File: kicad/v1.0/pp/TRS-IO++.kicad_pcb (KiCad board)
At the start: 2 copper layers, 145.7 x 107.8 mm, 104 parts, among them J1 TRS-80 M3 Pin Header, J10 Cassette Input, J11 Mini-DIN-6, J12 USB_B_Micro, J13 UART, J2 TRS-80 M1 Pin Header, J3 TRS-80 M3 Edge Connector, J4 TRS-80 M1 Edge Connector, J5 Conn_02x06_Odd_Even, J6 Cassette Output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

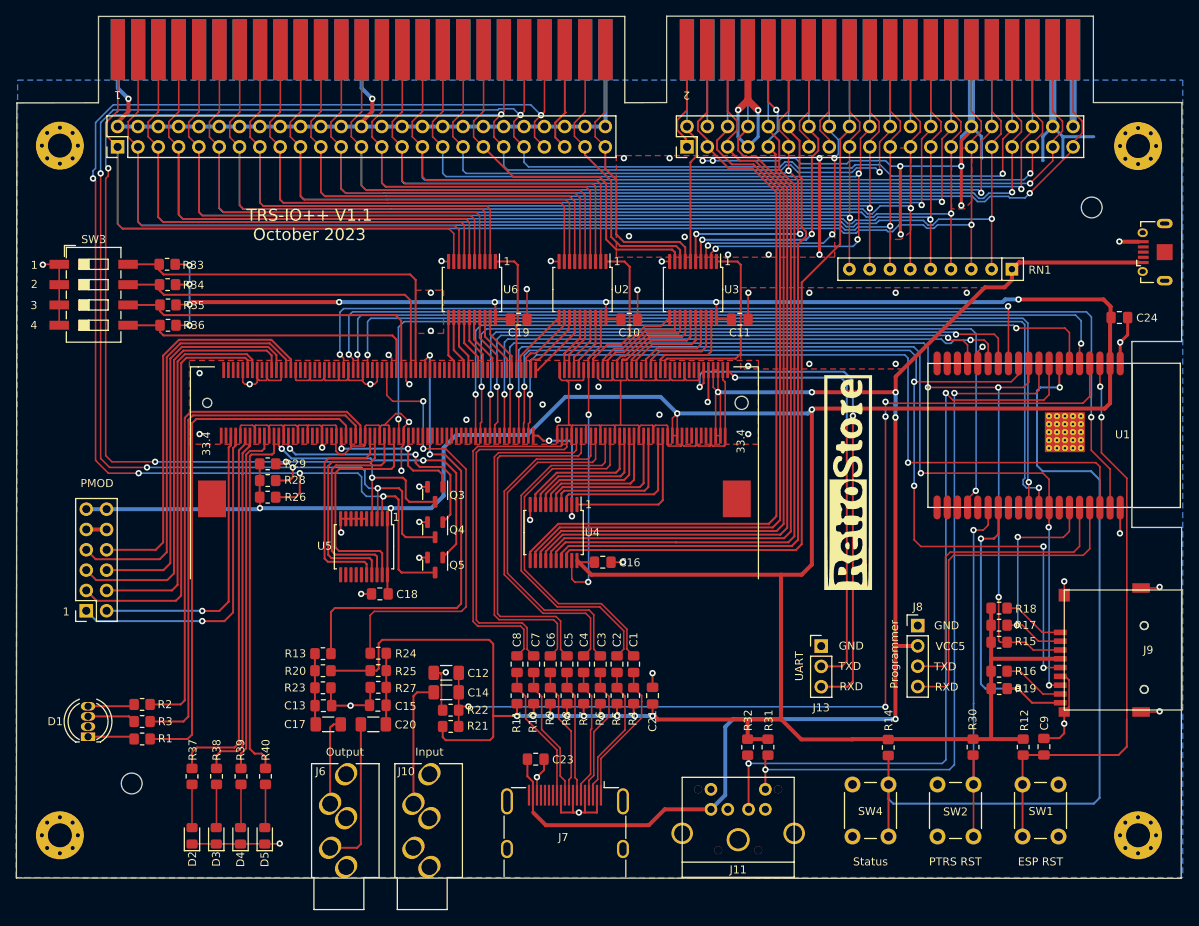
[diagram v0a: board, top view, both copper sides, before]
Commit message: Custom TRS-IO++ PCB (incomplete, no video)
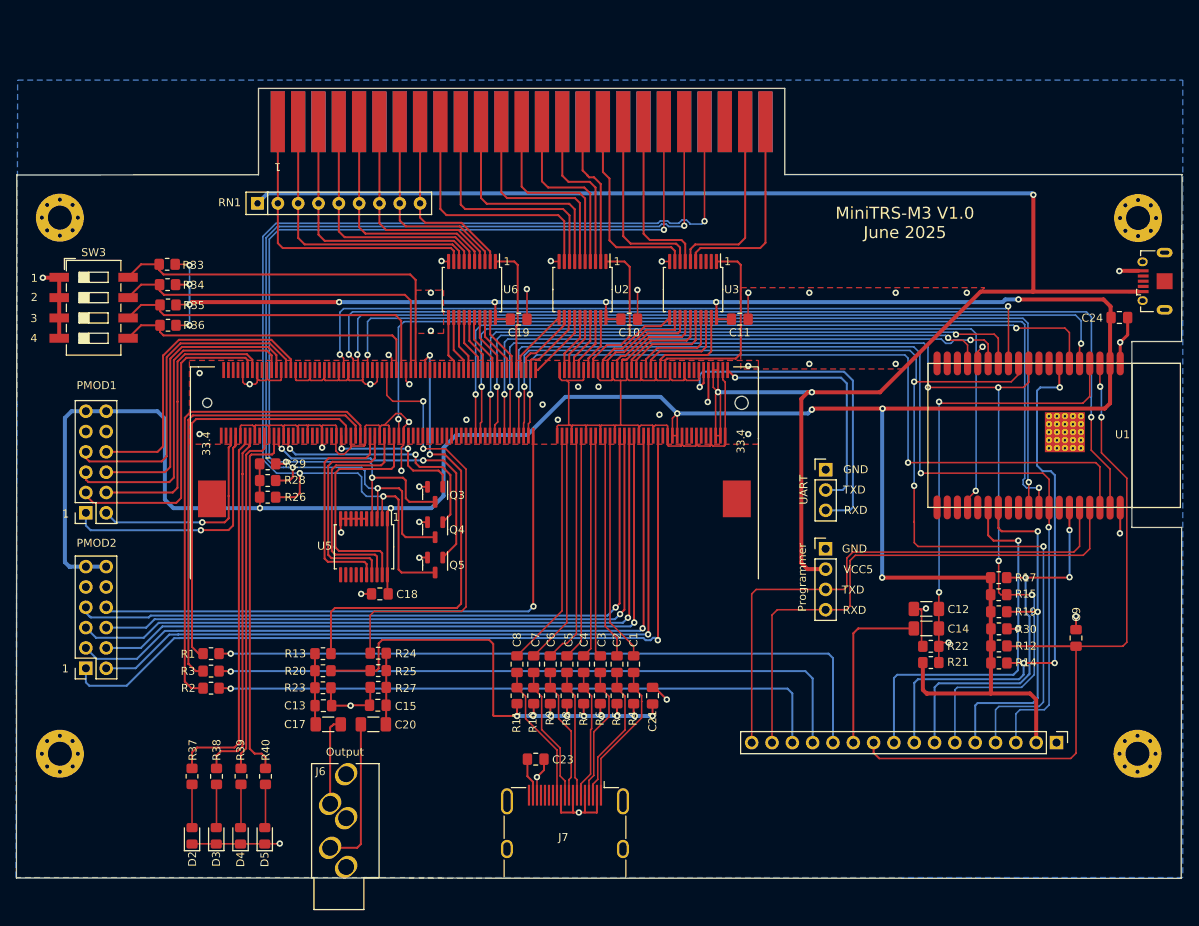
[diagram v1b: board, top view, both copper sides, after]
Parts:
- removed C16: 0.1uF, Capacitor_SMD:C_0805_2012Metric_Pad1.18x1.45mm_HandSolder
- removed D1: LED_RKBG, LED_THT:LED_D5.0mm-4_RGB
- removed G***, G1: LOGO, LOGO
- removed H5, H6: MountingHole, PocketTRS_Connectors:Alignment_Hole_2.6mm
- removed J10: Cassette Input, PocketTRS_Connectors:Jack_3.5mm_CUI_SJ1-3535NG_Horizontal_CircularHoles
- removed J11: Mini-DIN-6, PocketTRS_Connectors:minidin_6_ps2_pcb_mount
- removed J4: TRS-80 M1 Edge Connector, trs-io-m1:TRSEDGE
- removed J9: SD_Card, PocketTRS_Connectors:TFP09-2-12B
- removed R16, R18: 10K, Resistor_SMD:R_0805_2012Metric_Pad1.20x1.40mm_HandSolder
- removed R31, R32: 2K, Resistor_SMD:R_0805_2012Metric_Pad1.20x1.40mm_HandSolder
- removed SW1: ESP_RESET, Button_Switch_THT:SW_PUSH_6mm
- removed SW2: PTRS_RESET, Button_Switch_THT:SW_PUSH_6mm
- removed SW4: TRS_IO_STATUS, Button_Switch_THT:SW_PUSH_6mm
- removed U4: 74LVC245, trs-io-m3:SSOP-20_5.3x7.2mm_P0.65mm_slim
- J1: value TRS-80 M3 Pin Header -> Conn_02x06_Odd_Even; footprint Connector_PinHeader_2.54mm:PinHeader_2x25_P2.54mm_Vertical -> Connector_PinSocket_2.54mm:PinSocket_2x06_P2.54mm_Vertical
- J2: value TRS-80 M1 Pin Header -> Conn_01x16; footprint Connector_PinHeader_2.54mm:PinHeader_2x20_P2.54mm_Vertical -> Connector_PinHeader_2.54mm:PinHeader_1x16_P2.54mm_Vertical
- moved RN1 94.7 mm to (90.7, 62.5), turned to 0 degrees
- moved J2 87.6 mm to (190.6, 129.9), turned to -90 degrees
- moved J1 65.3 mm to (69.3, 120.6), turned to 180 degrees
- moved C12 60.5 mm to (174.3, 113.2)
- moved C14 60.5 mm to (174.3, 115.6)
- moved R21 60.5 mm to (174.9, 119.9)
- moved R22 60.5 mm to (174.9, 117.9)
- moved J13 22.1 mm to (161.7, 95.8)
- moved J3 21.9 mm to (132.0, 52.3)
- moved R14 17.4 mm to (183.4, 119.9), turned to 0 degrees
- moved R30 15.1 mm to (183.4, 115.7), turned to 0 degrees
- moved J8 15.0 mm to (161.7, 105.7)
- moved C9 14.2 mm to (193.0, 116.8)
- moved R1 13.7 mm to (84.9, 118.8), turned to 0 degrees
- moved R12 13.0 mm to (183.4, 117.8), turned to 0 degrees
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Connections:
- net PMOD_IO1 renamed PMOD1_IO1
- net PMOD_IO2 renamed PMOD1_IO2
- net PMOD_IO3 renamed PMOD1_IO3
- net PMOD_IO4 renamed PMOD1_IO4
- net PMOD_IO5 renamed PMOD1_IO5
- net PMOD_IO6 renamed PMOD1_IO6
- net PMOD_IO7 renamed PMOD1_IO7
- net PMOD_IO8 renamed PMOD1_IO8
- C14 pad 1: Net-(C14-Pad1) -> IF_CASS_IN
- Conn1 pad 30: _A8 -> PMOD2_IO1
- Conn1 pad 33: _IN_N -> _RD_N
- Conn1 pad 34: _A11 -> PMOD2_IO5
- Conn1 pad 35: _RD_N -> _WR_N
- Conn1 pad 36: _A14 -> PMOD2_IO2
- Conn1 pad 39: _WR_N -> _RAS_N
- Conn1 pad 40: _A15 -> PMOD2_IO6
- Conn1 pad 41: _OUT_N -> _IOREQ_N
- Conn1 pad 42: _A13 -> PMOD2_IO3
- Conn1 pad 44: _A12 -> PMOD2_IO7
- Conn1 pad 45: _RAS_N -> _M1_N
- Conn1 pad 46: _A10 -> PMOD2_IO4
- Conn1 pad 47: _IOREQ_N -> _RESET_N
- Conn1 pad 51: _M1_N -> _OUT_N
- Conn1 pad 53: _RESET_N -> _IN_N
- Conn1 pad 74: _A9 -> PMOD2_IO8
- Conn1 pad 78: SCK -> IF_SD_SCK
- Conn1 pad 80: MISO -> IF_SD_MISO
- Conn1 pad 84: MOSI -> IF_SD_MOSI
- J1 pad 1: D0 -> PMOD2_IO1
- J1 pad 11: D5 -> +3V3
- J1 pad 12: GND -> +3V3
- J1 pad 2: GND -> PMOD2_IO5
- J1 pad 3: D1 -> PMOD2_IO2
- J1 pad 4: GND -> PMOD2_IO6
- J1 pad 5: D2 -> PMOD2_IO3
- J1 pad 6: GND -> PMOD2_IO7
- J1 pad 7: D3 -> PMOD2_IO4
- J1 pad 8: GND -> PMOD2_IO8
- J1 pad 9: D4 -> GND
- J2 pad 1: SYSRES_N -> GND
- J2 pad 10: A11 -> ESP_RESET
- J2 pad 11: OUT_N -> IF_CASS_IN
- J2 pad 12: A8 -> IF_LED_RED
- J2 pad 13: INTACK_N -> IF_LED_BLUE
- J2 pad 14: WR_N -> IF_LED_GREEN
- J2 pad 15: MUX -> IF_RXD0
- J2 pad 16: RD_N -> IF_TXD0
- J2 pad 2: RAS_N -> +3V3
- J2 pad 3: A10 -> IF_SD_MISO
- J2 pad 4: CAS_N -> IF_SD_SCK
- J2 pad 5: A13 -> CD_SD
- J2 pad 6: A12 -> IF_SD_MOSI
- J2 pad 7: GND -> CS_SD
- J2 pad 8: A15 -> IF_BTN_TRSIO_STATUS
- J2 pad 9: A14 -> ID0
- J8 pad 3: RXD0 -> IF_TXD0
- J8 pad 4: TXD0 -> IF_RXD0
- R1 pad 2: Net-(D1-RA) -> IF_LED_RED
- R14 pad 2: STATUS -> IF_BTN_TRSIO_STATUS
- R15 pad 2: MOSI -> IF_SD_MOSI
- R2 pad 2: Net-(D1-GA) -> IF_LED_GREEN
- R3 pad 2: Net-(D1-BA) -> IF_LED_BLUE
- RN1 pad 2: D2 -> D0
- RN1 pad 3: D0 -> D1
- RN1 pad 4: D5 -> D2
- RN1 pad 6: D6 -> D4
- RN1 pad 7: D1 -> D5
- RN1 pad 8: D7 -> D6
- RN1 pad 9: D4 -> D7
- U1 pad 10: MOSI -> IF_SD_MOSI
- U1 pad 11: SCK -> IF_SD_SCK
- U1 pad 31: MISO -> IF_SD_MISO
- U1 pad 34: RXD0 -> IF_TXD0
- U1 pad 35: TXD0 -> IF_RXD0
- U1 pad 7: STATUS -> IF_BTN_TRSIO_STATUS
- U1 pad 8: PS2_DATA -> unconnected-(U1-IO32-Pad8)
- U1 pad 9: PS2_CLK -> unconnected-(U1-IO33-Pad9)
- U3 pad 11: _RESET_N -> _IN_N
- U3 pad 12: _M1_N -> _OUT_N
- U3 pad 13: _IOREQ_N -> _RESET_N
- U3 pad 14: _RAS_N -> _M1_N
- U3 pad 15: _OUT_N -> _IOREQ_N
- U3 pad 16: _WR_N -> _RAS_N
- U3 pad 17: _RD_N -> _WR_N
- U3 pad 18: _IN_N -> _RD_N
- U3 pad 2: IN_N -> RD_N
- U3 pad 3: RD_N -> WR_N
- U3 pad 4: WR_N -> RAS_N
- U3 pad 5: OUT_N -> IOREQ_N
- U3 pad 6: RAS_N -> M1_N
- U3 pad 7: IOREQ_N -> RESET_N
- U3 pad 8: M1_N -> OUT_N
- U3 pad 9: RESET_N -> IN_N
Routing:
- net GND: track 508.6 -> 271.2 mm, vias 71 -> 48
- net D0: track 215.2 -> 38.9 mm, vias 1 -> 0
- net D2: track 207.5 -> 34.5 mm, vias 1 -> 0
- net D1: track 199.5 -> 36.6 mm, vias 1 -> 0
- net D3: track 194.5 -> 32.3 mm, vias 1 -> 0
- net D5: track 187.0 -> 28.0 mm, vias 1 -> 0
- net D6: track 177.7 -> 25.9 mm, vias 1 -> 0
- net D4: track 179.8 -> 30.2 mm, vias 1 -> 0
- net A2: track 174.1 -> 28.4 mm, vias 1 -> 0
- net D7: track 167.7 -> 23.7 mm, vias 1 -> 0
- net IF_SD_SCK: track 0.00 -> 142.9 mm, vias 0 -> 4
- net IF_SD_MOSI: track 0.00 -> 141.7 mm, vias 0 -> 5
- net A3: track 164.7 -> 26.5 mm, vias 1 -> 0
- net A0: track 169.1 -> 32.1 mm, vias 1 -> 0
- net A1: track 166.3 -> 30.3 mm, vias 1 -> 0
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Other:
- board size 145.7 x 107.8 mm -> 145.7 x 98.7 mm
- board text added: "MiniTRS-M3 V1.0 June 2025"
- board text added: "PMOD1"
- board text added: "PMOD2"
- board text removed: "ESP RST"
- board text removed: "Input"
- board text removed: "PMOD"
- board text removed: "PTRS RST"
- board text removed: "Status"
- board text removed: "TRS-IO++ V1.1 October 2023"

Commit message: Updates to KiCad schematics/layout
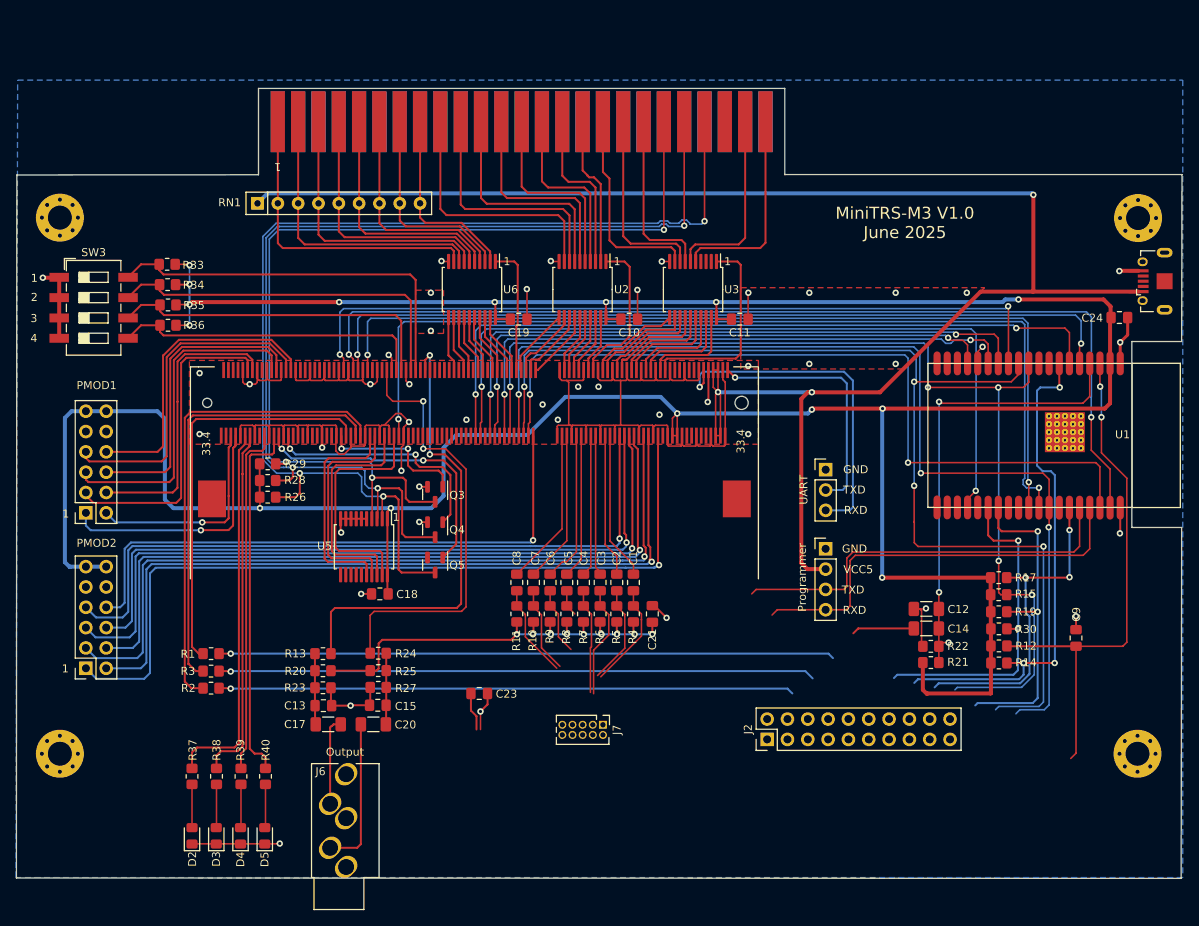
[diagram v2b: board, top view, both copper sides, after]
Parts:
- J2: value Conn_01x16 -> Interface Connector; footprint Connector_PinHeader_2.54mm:PinHeader_1x16_P2.54mm_Vertical -> Connector_PinHeader_2.54mm:PinHeader_2x10_P2.54mm_Vertical
- J7: value HDMI_A -> HDMI; footprint trs-io-m1:HDMI_A_Molex_208658-1001_Horizontal -> Connector_PinHeader_1.27mm:PinHeader_2x05_P1.27mm_Vertical
- moved J2 36.2 mm to (154.4, 129.5), turned to 90 degrees
- moved J7 13.0 mm to (133.9, 127.7)
- moved C23 10.8 mm to (118.4, 123.7)
- moved C1 10.2 mm to (137.7, 109.9)
- moved C5 10.2 mm to (129.4, 109.9)
- moved C2 10.2 mm to (135.6, 109.9)
- moved C3 10.2 mm to (133.6, 109.9)
- moved C4 10.2 mm to (131.5, 109.9)
- moved C6 10.2 mm to (127.3, 109.9)
- moved C7 10.2 mm to (125.2, 109.9)
- moved C8 10.2 mm to (123.1, 109.9)
- moved C21 10.2 mm to (140.1, 113.8)
- moved R4 10.2 mm to (137.7, 113.8)
- moved R8 10.2 mm to (129.4, 113.8)
- moved R10 10.2 mm to (125.2, 113.8)
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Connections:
- J2 pad 1: GND -> IF_SD_MISO
- J2 pad 10: ESP_RESET -> IF_LED_RED
- J2 pad 11: IF_CASS_IN -> IF_BTN_TRSIO_STATUS
- J2 pad 12: IF_LED_RED -> IF_CASS_IN
- J2 pad 13: IF_LED_BLUE -> ID0
- J2 pad 14: IF_LED_GREEN -> ESP_RESET
- J2 pad 15: IF_RXD0 -> unconnected-(J2-Pin_15-Pad15)
- J2 pad 16: IF_TXD0 -> unconnected-(J2-Pin_16-Pad16)
- J2 pad 2: +3V3 -> IF_TXD0
- J2 pad 3: IF_SD_MISO -> IF_SD_SCK
- J2 pad 4: IF_SD_SCK -> IF_RXD0
- J2 pad 6: IF_SD_MOSI -> IF_LED_GREEN
- J2 pad 7: CS_SD -> IF_SD_MOSI
- J2 pad 8: IF_BTN_TRSIO_STATUS -> IF_LED_BLUE
- J2 pad 9: ID0 -> CS_SD
- J7 pad 10: /CK+ -> GND
- J7 pad 2: GND -> /D2-
- J7 pad 3: /D2- -> /D1+
- J7 pad 4: /D1+ -> /D1-
- J7 pad 5: GND -> /D0+
- J7 pad 6: /D1- -> /D0-
- J7 pad 7: /D0+ -> /CK+
- J7 pad 8: GND -> /CK-
- J7 pad 9: /D0- -> +5V
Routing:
- net ESP_RESET: track 91.9 -> 65.8 mm
- net +3V3: track 492.3 -> 471.9 mm
- net IF_TXD0: track 69.0 -> 50.4 mm
- net IF_RXD0: track 67.6 -> 51.6 mm
- net GND: track 271.2 -> 257.0 mm, vias 48 -> 46
- net IF_CASS_IN: track 21.5 -> 7.82 mm
- net /D0+: track 15.9 -> 3.31 mm
- net IF_LED_RED: track 87.6 -> 77.0 mm
- net HDMI_TX1_P: track 27.8 -> 17.3 mm
- net HDMI_TX2_N: track 28.2 -> 17.9 mm
- net HDMI_TX2_P: track 28.7 -> 18.5 mm
- net HDMI_TXC_N: track 29.9 -> 19.7 mm
- net HDMI_TX1_N: track 27.9 -> 17.7 mm
- net HDMI_TXC_P: track 29.2 -> 19.0 mm
- net HDMI_TX0_N: track 29.2 -> 19.0 mm
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
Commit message: First version of PCB (without HDMI)
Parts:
- removed C13: 100N, Capacitor_SMD:C_0805_2012Metric_Pad1.18x1.45mm_HandSolder
- removed C17: 10U, Capacitor_SMD:C_1206_3216Metric_Pad1.33x1.80mm_HandSolder
- removed D4, D5: LED, LED_SMD:LED_0805_2012Metric_Pad1.15x1.40mm_HandSolder
- removed J12: USB_B_Micro, PocketTRS_Connectors:USBmicro-B
- removed R13: 270R, Resistor_SMD:R_0805_2012Metric_Pad1.20x1.40mm_HandSolder
- removed R20, R23: 300R, Resistor_SMD:R_0805_2012Metric_Pad1.20x1.40mm_HandSolder
- added C16: 1U, Capacitor_SMD:C_0805_2012Metric_Pad1.18x1.45mm_HandSolder, F.Cu at (167.7, 73.7)
- added C22: 150, Capacitor_SMD:C_0805_2012Metric_Pad1.18x1.45mm_HandSolder, F.Cu at (176.0, 73.7)
- added C25: 1U, Capacitor_SMD:C_0805_2012Metric_Pad1.18x1.45mm_HandSolder, F.Cu at (162.2, 66.1)
- added C26: 1U, Capacitor_SMD:C_0805_2012Metric_Pad1.18x1.45mm_HandSolder, F.Cu at (160.0, 66.1)
- added C27: 150, Capacitor_SMD:C_0805_2012Metric_Pad1.18x1.45mm_HandSolder, F.Cu at (178.1, 66.3)
- added J4: SPEAKER, Connector_PinHeader_2.54mm:PinHeader_1x02_P2.54mm_Vertical, F.Cu at (183.2, 67.8)
- added J9: LED4, Connector_PinHeader_2.54mm:PinHeader_1x02_P2.54mm_Vertical, F.Cu at (101.7, 128.2)
- added R16: 20k, Resistor_SMD:R_0805_2012Metric_Pad1.20x1.40mm_HandSolder, F.Cu at (178.3, 73.6)
- added R18: 10k, Resistor_SMD:R_0805_2012Metric_Pad1.20x1.40mm_HandSolder, F.Cu at (165.5, 73.7)
- added R31: 20k, Resistor_SMD:R_0805_2012Metric_Pad1.20x1.40mm_HandSolder, F.Cu at (175.9, 66.3)
- added RV1: 20k, Potentiometer_SMD:Potentiometer_Bourns_TC33X_Vertical, F.Cu at (171.7, 73.7)
- added U4: LM4991MM, Package_SO:SOIC-8_3.9x4.9mm_P1.27mm, F.Cu at (169.0, 66.1)
- J6: value Cassette Output -> LED3; footprint PocketTRS_Connectors:Jack_3.5mm_CUI_SJ1-3535NG_Horizontal_CircularHoles -> Connector_PinHeader_2.54mm:PinHeader_1x02_P2.54mm_Vertical
- moved J6 17.8 mm to (97.1, 128.2), turned to 0 degrees
- moved D3 14.4 mm to (76.7, 130.1), turned to -90 degrees
- moved D2 11.7 mm to (79.8, 130.1), turned to -90 degrees
- moved R37 3.97 mm to (82.5, 130.1)
- moved R38 3.97 mm to (85.6, 130.1)
- moved R39 3.97 mm to (88.7, 130.1)
- moved R40 3.97 mm to (91.7, 130.1)
- moved C15 3.86 mm to (109.6, 125.2)
- moved C20 3.86 mm to (109.1, 127.6)
- moved R24 3.86 mm to (109.7, 118.7)
- moved R25 3.86 mm to (109.7, 120.9)
- moved R27 3.86 mm to (109.7, 123.0)
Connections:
- C20 pad 1: Net-(C20-Pad1) -> IF_CASS_OUT
- J2 pad 1: IF_SD_MISO -> unconnected-(J2-Pin_1-Pad1)
- J2 pad 10: IF_LED_RED -> ID0
- J2 pad 11: IF_BTN_TRSIO_STATUS -> IF_SD_MISO
- J2 pad 12: IF_CASS_IN -> IF_BTN_TRSIO_STATUS
- J2 pad 13: ID0 -> IF_SD_SCK
- J2 pad 14: ESP_RESET -> CS_SD
- J2 pad 15: unconnected-(J2-Pin_15-Pad15) -> CD_SD
- J2 pad 16: unconnected-(J2-Pin_16-Pad16) -> IF_SD_MOSI
- J2 pad 2: IF_TXD0 -> IF_CASS_OUT
- J2 pad 3: IF_SD_SCK -> IF_LED_GREEN
- J2 pad 4: IF_RXD0 -> IF_TXD0
- J2 pad 5: CD_SD -> IF_LED_BLUE
- J2 pad 6: IF_LED_GREEN -> IF_RXD0
- J2 pad 7: IF_SD_MOSI -> IF_LED_RED
- J2 pad 8: IF_LED_BLUE -> IF_CASS_IN
- J2 pad 9: CS_SD -> ESP_RESET
- R39 pad 2: Net-(D4-A) -> Net-(J6-Pin_1)
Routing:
- net CASS_OUT: track 54.7 -> 148.3 mm, vias 2 -> 4
- net CASS_OUT2: track 57.7 -> 0.00 mm, vias 2 -> 0
- net IF_CASS_OUT: track 0.00 -> 52.6 mm
- net +5V: track 215.9 -> 170.7 mm
- net ESP_RESET: track 65.8 -> 98.2 mm
- net IF_SD_MISO: track 125.6 -> 153.4 mm, vias 3 -> 4
- net IF_SD_SCK: track 138.7 -> 160.4 mm, vias 4 -> 5
- net Net-(J4-Pin_2): track 0.00 -> 21.2 mm
- net Net-(C20-Pad1): track 19.0 -> 0.00 mm
- net Net-(U4--): track 0.00 -> 16.7 mm
- net CD_SD: track 40.6 -> 56.3 mm, vias 2 -> 3
- net Net-(J4-Pin_1): track 0.00 -> 15.0 mm
- net /CK-: track 11.8 -> 25.7 mm
- net IF_CASS_IN: track 7.82 -> 21.6 mm
- net +3V3: track 471.9 -> 484.0 mm
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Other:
- board size 145.7 x 98.7 mm -> 145.7 x 88.6 mm
- board text added: "LED1"
- board text added: "LED2"
- board text added: "Speaker"
- board text removed: "Output"
